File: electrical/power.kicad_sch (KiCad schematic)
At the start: 58 parts

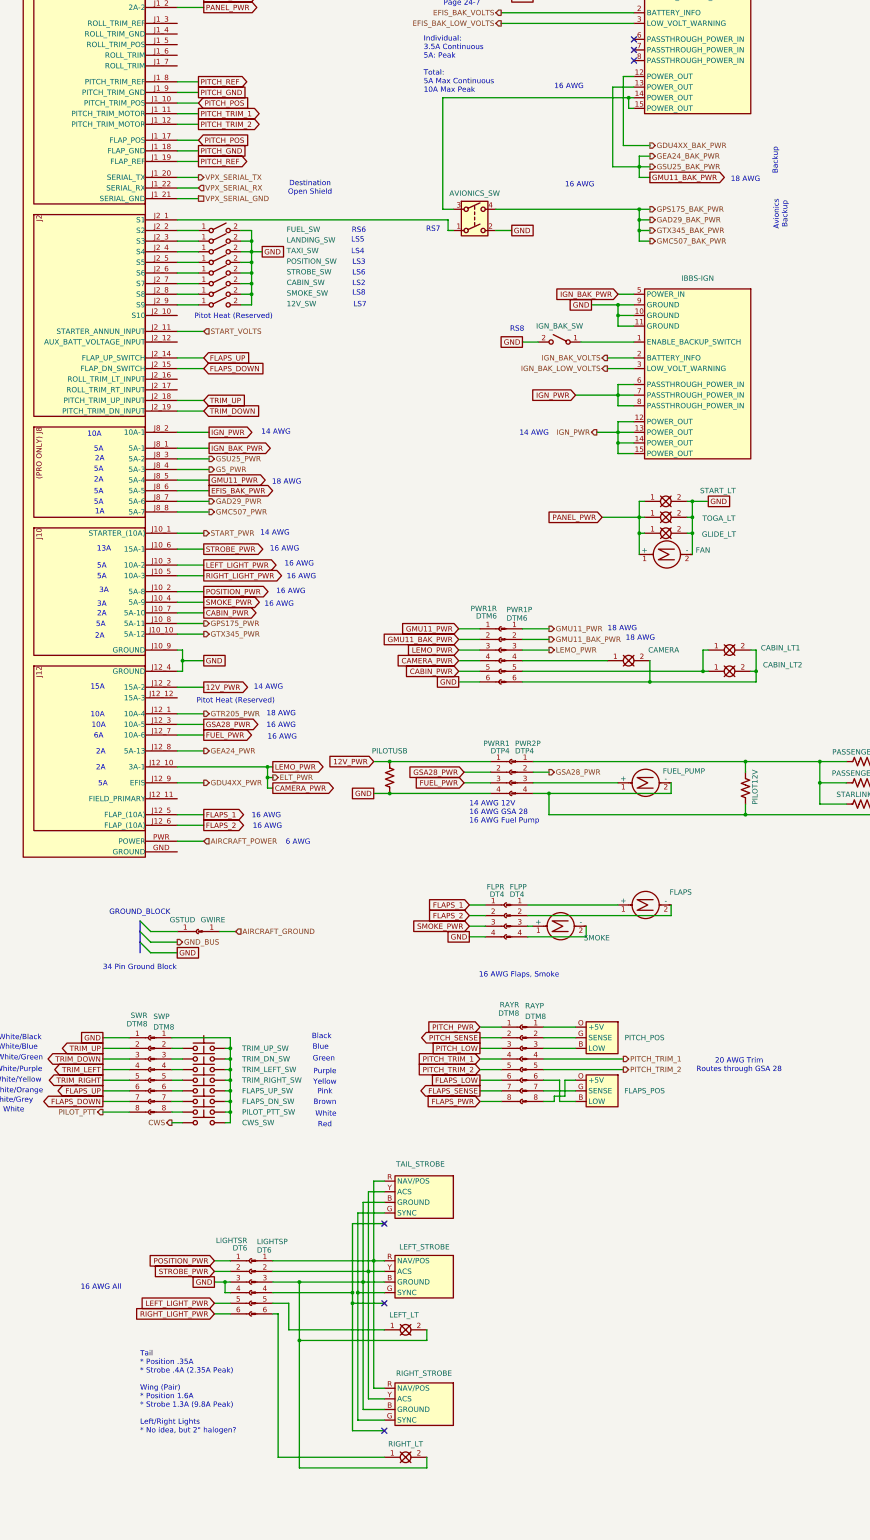
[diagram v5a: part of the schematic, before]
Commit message: Moved Pitch and Flaps to their own connector. Fixed Ref/Gnd/Low for Ray Allen pitch & flaps sensors.
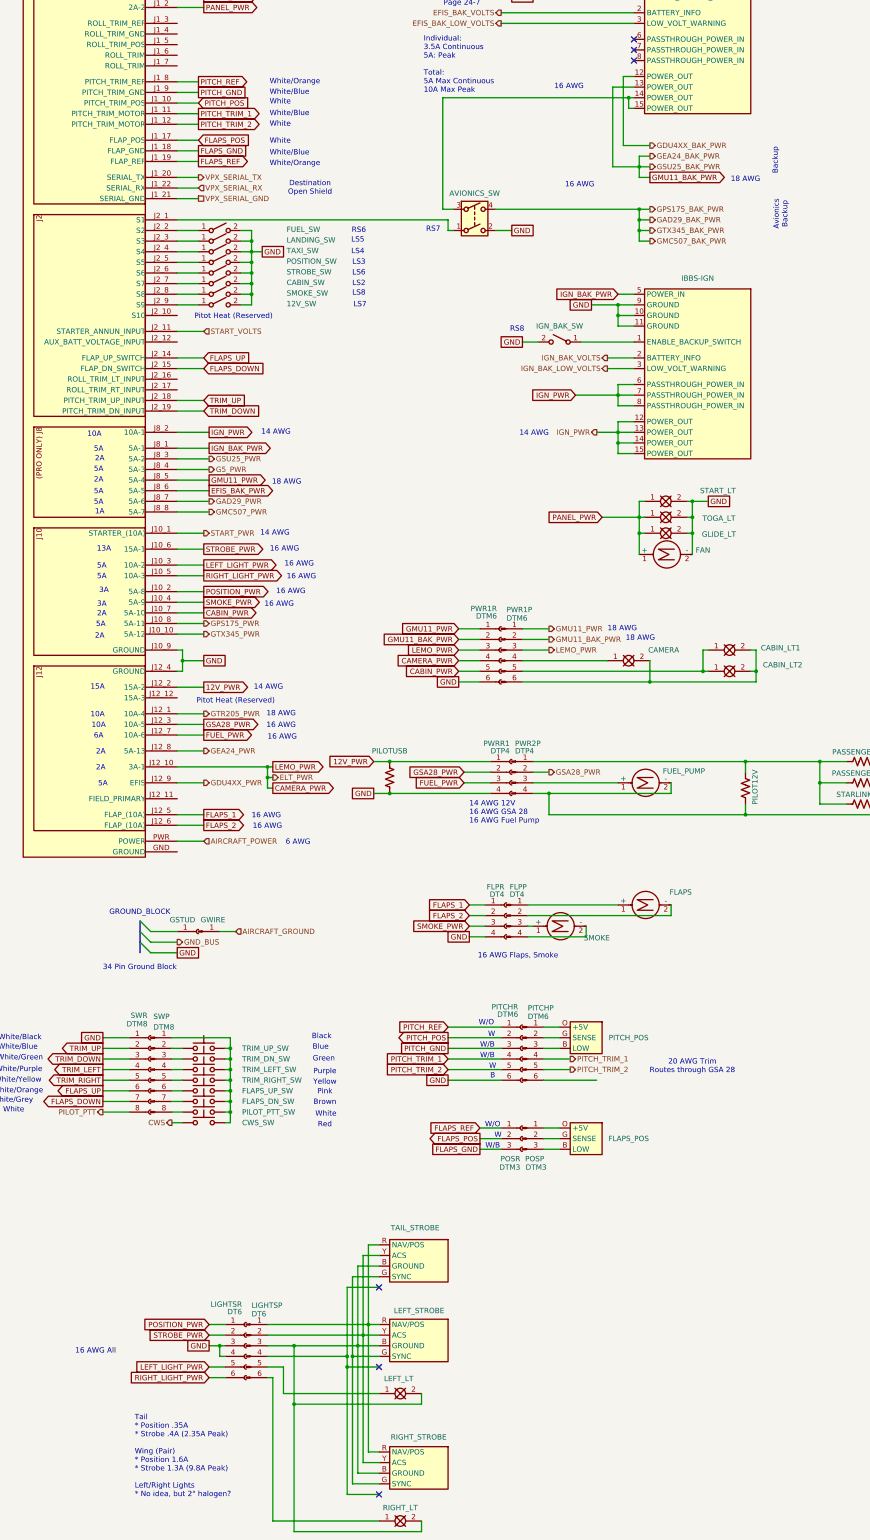
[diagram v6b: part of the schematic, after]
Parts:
- removed RAYP: DTM8, symbol Connector:Conn_01x08_Pin
- removed RAYR: DTM8, symbol Connector:Conn_01x08_Socket
- added PITCHP: DTM6, symbol Connector:Conn_01x06_Pin
- added PITCHR: DTM6, symbol Connector:Conn_01x06_Socket
- added POSP: DTM3, symbol Connector:Conn_01x03_Pin
- added POSR: DTM3, symbol Connector:Conn_01x03_Socket
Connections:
- net GND: now also PITCHR.6 (Pin_6)
- net PITCH_GND: now also PITCHR.3 (Pin_3); no longer VPX.J1_18 (FLAP_GND)
- net PITCH_POS: now also PITCHR.2 (Pin_2); no longer VPX.J1_17 (FLAP_POS)
- net PITCH_REF: now also PITCHR.1 (Pin_1); no longer VPX.J1_19 (FLAP_REF)
- net PITCH_TRIM_1: now also PITCHP.4 (Pin_4), PITCHR.4 (Pin_4)
- net PITCH_TRIM_2: now also PITCHP.5 (Pin_5), PITCHR.5 (Pin_5)
- net at PITCH_POS.O (+5V): now also PITCHP.1 (Pin_1)
- net at PITCH_POS.G (SENSE): now also PITCHP.2 (Pin_2)
- net at PITCH_POS.B (LOW): now also PITCHP.3 (Pin_3)
- net at FLAPS_POS.B (LOW): now also POSP.3 (Pin_3)
- net at FLAPS_POS.G (SENSE): now also POSP.2 (Pin_2)
- net at FLAPS_POS.O (+5V): now also POSP.1 (Pin_1)
- new net FLAPS_GND: POSR.3 (Pin_3), VPX.J1_18 (FLAP_GND)
- new net FLAPS_POS: POSR.2 (Pin_2), VPX.J1_17 (FLAP_POS)
- new net FLAPS_REF: POSR.1 (Pin_1), VPX.J1_19 (FLAP_REF)
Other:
- note added: "B"
- note added: "W"
- note added: "W/B"
- note added: "W/O"
- moved on the sheet: FLAPS_POS, LEFT_LT, LEFT_STROBE, LIGHTSP, LIGHTSR, PITCH_POS, RIGHT_LT, RIGHT_STROBE, TAIL_STROBE

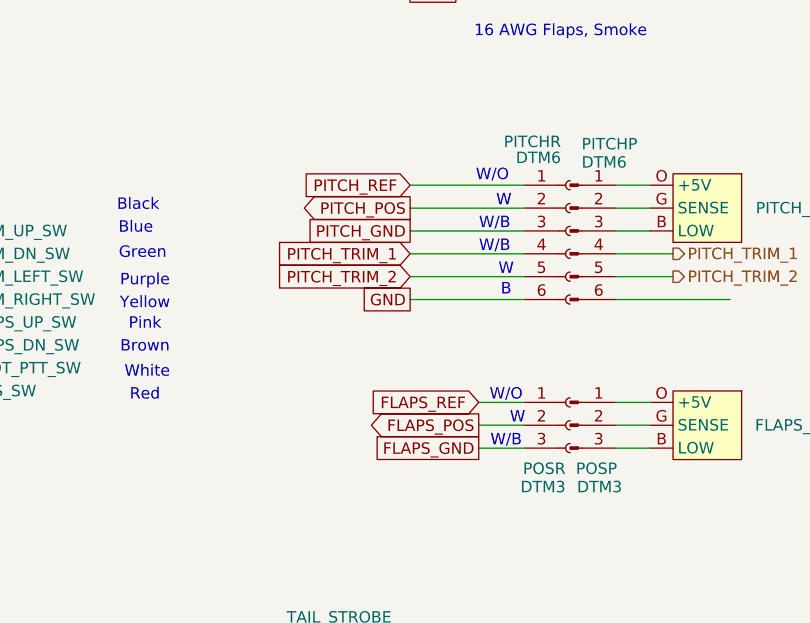
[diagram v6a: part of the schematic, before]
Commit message: Cosmetic change on pitch/flaps sensors
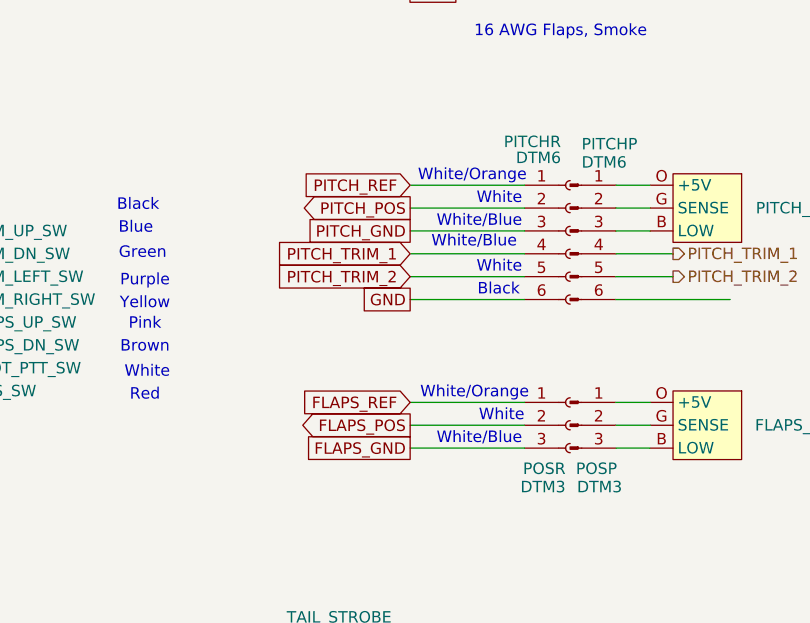
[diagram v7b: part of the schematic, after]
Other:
- note removed: "B"
- note removed: "W"
- note removed: "W/B"
- note removed: "W/O"
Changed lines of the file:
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@@
 		)
 	)
-	(text "W/O"
-		(exclude_from_sim no)
-		(at 132.588 298.958 0)
-		(effects
-			(font
-				(size 1.27 1.27)
-			)
-		)
-	)
 	(text "RS8"
 		(exclude_from_sim no)
@@
 		)
 	)
-	(text "W/B"
-		(exclude_from_sim no)
-		(at 132.588 304.038 0)
-		(effects
-			(font
-				(size 1.27 1.27)
-			)
-		)
-	)
 	(text "Backup"
 		(exclude_from_sim no)
@@
 		)
 	)
+	(text "White/Blue"
+		(exclude_from_sim no)
+		(at 134.366 303.784 0)
+		(effects
+			(font
+				(size 1.27 1.27)
+			)
+			(justify right)
+		)
+	)
 	(text "18 AWG"
 		(exclude_from_sim no)
@@
 		)
 	)
-	(text "W"
+	(text "White"
 		(exclude_from_sim no)
-		(at 132.588 284.988 0)
+		(at 134.366 284.734 0)
 		(effects
 			(font
 				(size 1.27 1.27)
 			)
+			(justify right)
 		)
 	)
-	(text "B"
+	(text "Black"
 		(exclude_from_sim no)
-		(at 132.588 287.274 0)
+		(at 134.112 287.274 0)
 		(effects
 			(font
 				(size 1.27 1.27)
 			)
+			(justify right)
 		)
 	)
@@
 		)
 	)
-	(text "W"
+	(text "White"
 		(exclude_from_sim no)
-		(at 132.334 277.368 0)
+		(at 134.366 277.114 0)
 		(effects
 			(font
 				(size 1.27 1.27)
 			)
+			(justify right)
 		)
 	)
@@
 		)
 	)
-	(text "W/B"
-		(exclude_from_sim no)
-		(at 131.318 279.908 0)
-		(effects
-			(font
-				(size 1.27 1.27)
-			)
-		)
-	)
-	(text "W"
+	(text "White/Blue"
 		(exclude_from_sim no)
-		(at 133.858 301.498 0)
+		(at 134.366 279.654 0)
 		(effects
 			(font
 				(size 1.27 1.27)
 			)
+			(justify right)
 		)
 	)
-	(text "W/O"
+	(text "White/Orange"
 		(exclude_from_sim no)
-		(at 131.064 274.574 0)
+		(at 134.874 274.574 0)
 		(effects
 			(font
 				(size 1.27 1.27)
 			)
+			(justify right)
 		)
 	)
@@
 		)
 	)
-	(text "W/B"
+	(text "White/Blue"
 		(exclude_from_sim no)
-		(at 131.318 282.448 0)
+		(at 129.032 281.94 0)
 		(effects
 			(font
@@
 		)
 	)
+	(text "White"
+		(exclude_from_sim no)
+		(at 134.62 301.244 0)
+		(effects
+			(font
+				(size 1.27 1.27)
+			)
+			(justify right)
+		)
+	)
 	(text "34 Pin Ground Block"
 		(exclude_from_sim no)
@@
 		)
 	)
+	(text "White/Orange"
+		(exclude_from_sim no)
+		(at 135.128 298.704 0)
+		(effects
+			(font
+				(size 1.27 1.27)
+			)
+			(justify right)
+		)
+	)
 	(text "Avionics\nBackup"
 		(exclude_from_sim no)
@@
 	(wire
 		(pts
-			(xy 129.54 302.26) (xy 134.62 302.26)
+			(xy 121.92 302.26) (xy 134.62 302.26)
 		)
 		(stroke
@@
 	(wire
 		(pts
-			(xy 129.54 304.8) (xy 134.62 304.8)
+			(xy 121.92 304.8) (xy 134.62 304.8)
 		)
 		(stroke
@@
 	(wire
 		(pts
-			(xy 129.54 299.72) (xy 134.62 299.72)
+			(xy 121.92 299.72) (xy 134.62 299.72)
 		)
 		(stroke
@@
 	(global_label "FLAPS_GND"
 		(shape passive)
-		(at 129.54 304.8 180)
+		(at 121.92 304.8 180)
 		(fields_autoplaced yes)
 		(effects
@@
 		)
 		(property "Intersheetrefs" "${INTERSHEET_REFS}"
-			(at 117.1432 304.8 0)
+			(at 109.5232 304.8 0)
 			(effects
 				(font
@@
 	(global_label "FLAPS_POS"
 		(shape output)
-		(at 129.54 302.26 180)
+		(at 121.92 302.26 180)
 		(fields_autoplaced yes)
 		(effects
@@
 		)
 		(property "Intersheetrefs" "${INTERSHEET_REFS}"
-			(at 116.0924 302.26 0)
+			(at 108.4724 302.26 0)
 			(effects
 				(font
@@
 	(global_label "FLAPS_REF"
 		(shape input)
-		(at 129.54 299.72 180)
+		(at 121.92 299.72 180)
 		(fields_autoplaced yes)
 		(effects
@@
 		)
 		(property "Intersheetrefs" "${INTERSHEET_REFS}"
-			(at 116.3948 299.72 0)
+			(at 108.7748 299.72 0)
 			(effects
 				(font

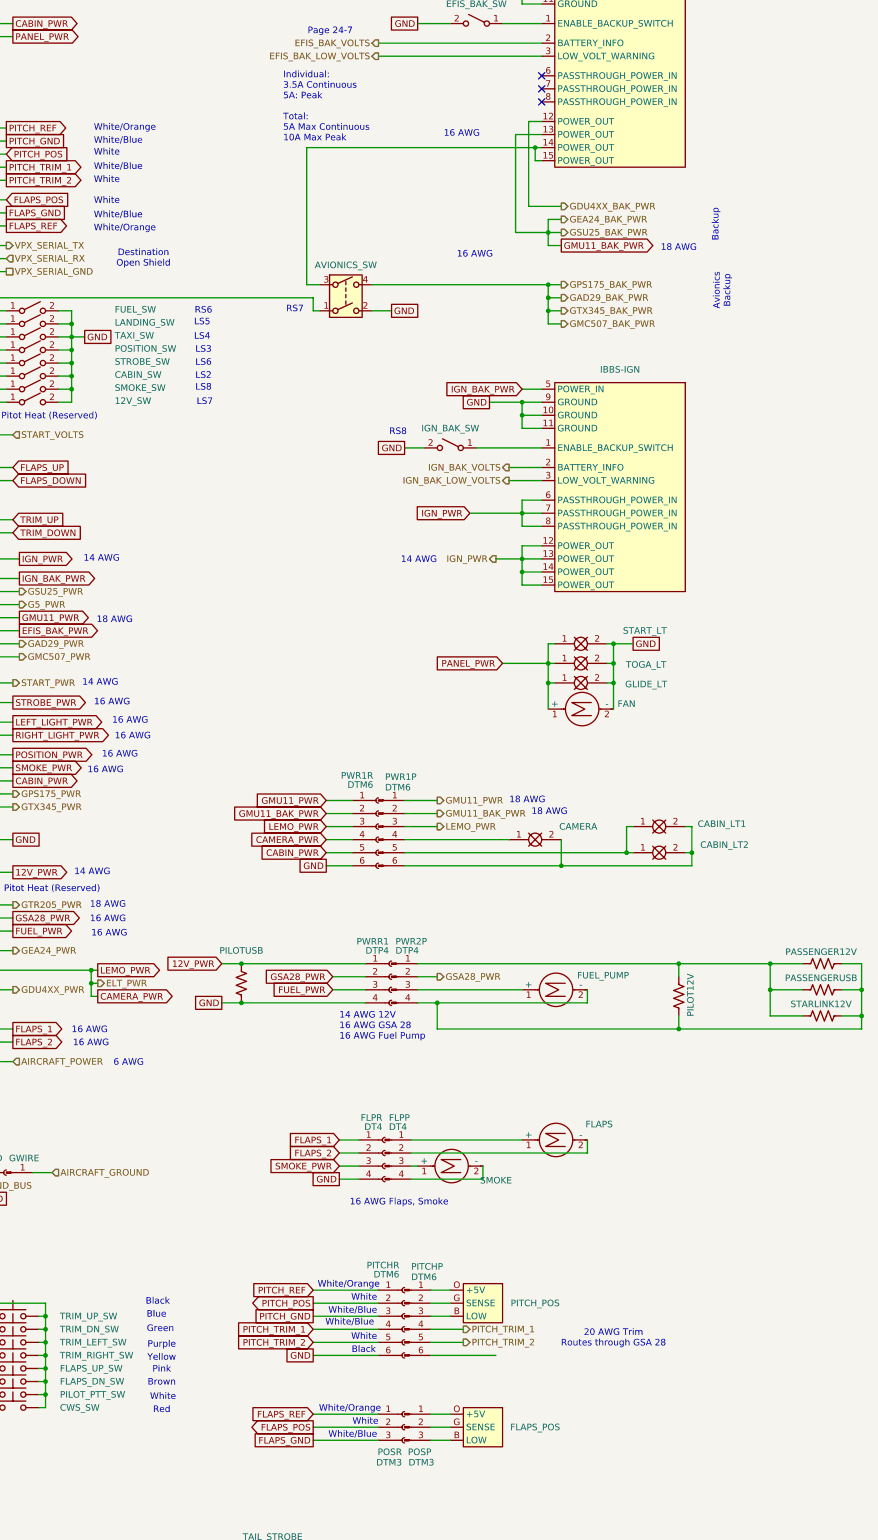
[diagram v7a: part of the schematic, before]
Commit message: Changed pin mapping for Flaps/Trim Sensors to match VP-X manual.
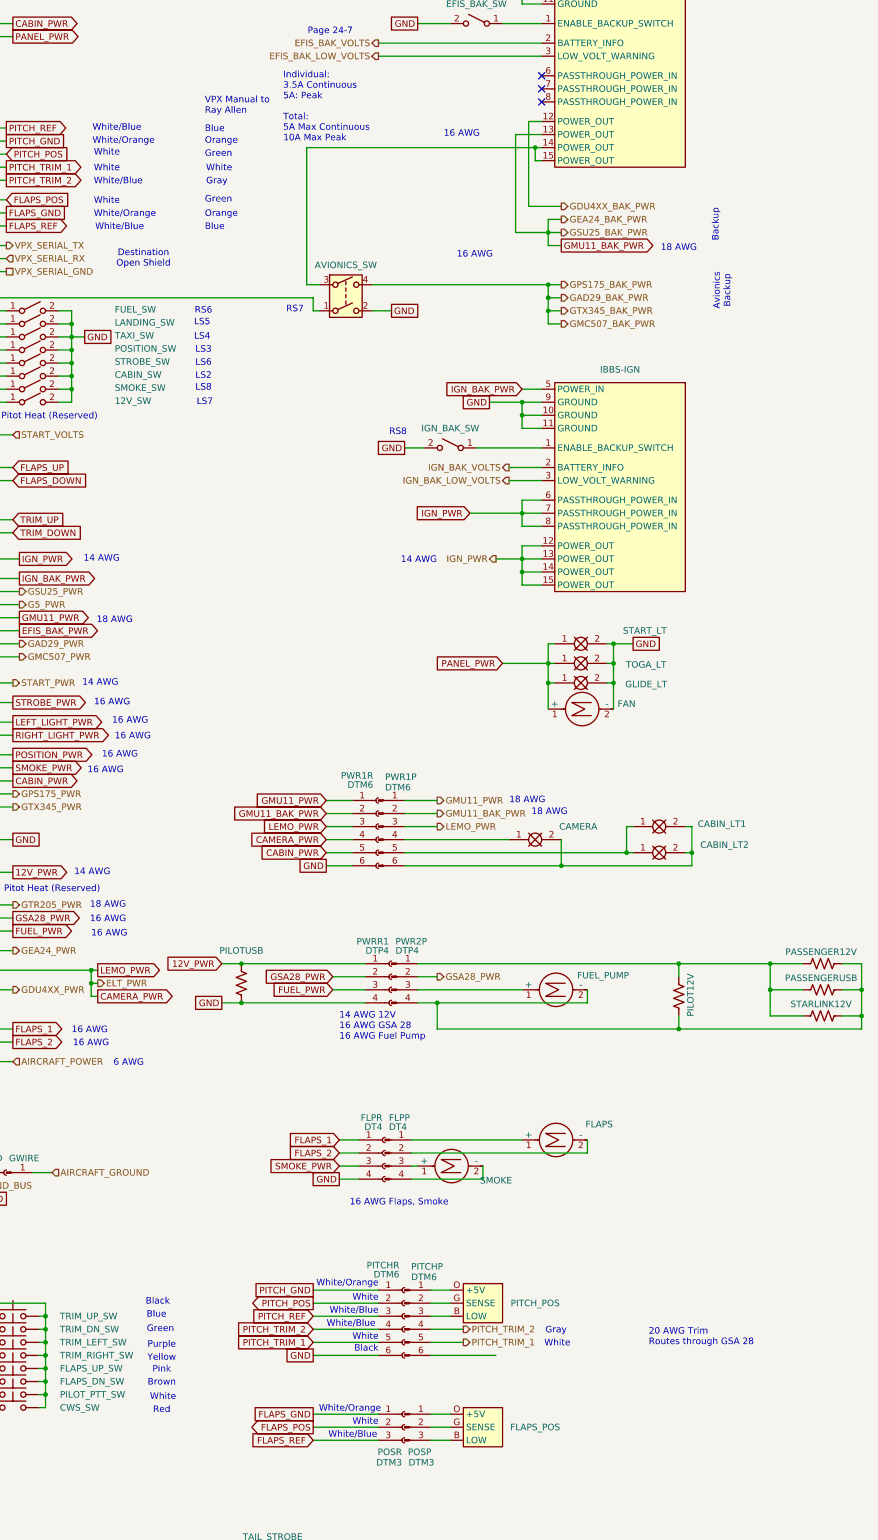
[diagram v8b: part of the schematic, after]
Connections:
- net FLAPS_GND: now also POSR.1 (Pin_1); no longer POSR.3 (Pin_3)
- net FLAPS_REF: now also POSR.3 (Pin_3); no longer POSR.1 (Pin_1)
- net PITCH_GND: now also PITCHR.1 (Pin_1); no longer PITCHR.3 (Pin_3)
- net PITCH_REF: now also PITCHR.3 (Pin_3); no longer PITCHR.1 (Pin_1)
- net PITCH_TRIM_1: now also PITCHP.5 (Pin_5), PITCHR.5 (Pin_5); no longer PITCHP.4 (Pin_4), PITCHR.4 (Pin_4)
- net PITCH_TRIM_2: now also PITCHP.4 (Pin_4), PITCHR.4 (Pin_4); no longer PITCHP.5 (Pin_5), PITCHR.5 (Pin_5)
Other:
- note added: "Gray"
- note added: "Orange"
- note added: "VPX Manual to Ray Allen"
